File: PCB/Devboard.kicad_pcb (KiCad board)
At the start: 2 copper layers, 21 x 51 mm, 34 parts, among them J1 USB_C_Receptacle_USB2.0_14P, J2 Conn_01x20, J3 Conn_01x20, J4 Conn_01x03, SW1 SW_Push, U1 RP2040, U2 NCP1117-3.3_SOT223, U3 W25Q16JVZPIQ TR, Y1 12 MHz

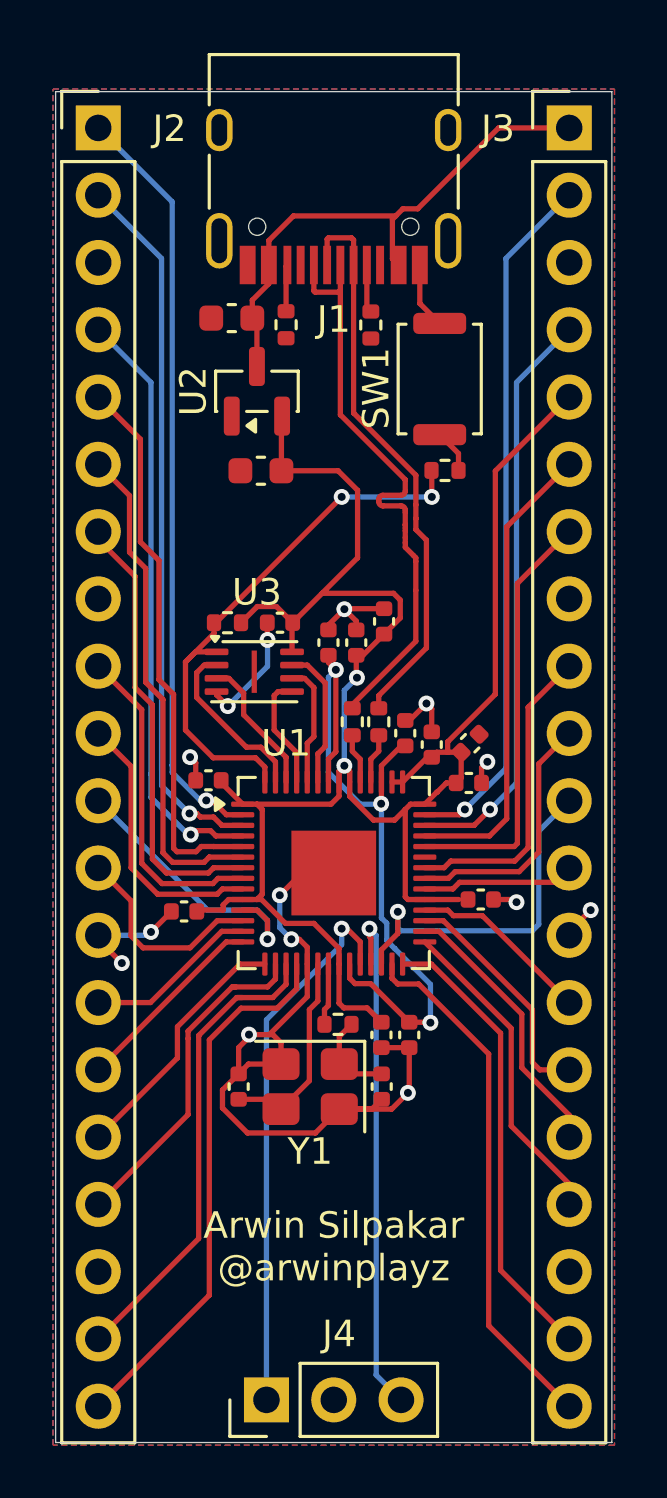
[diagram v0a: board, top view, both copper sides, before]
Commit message: added temperature sensor
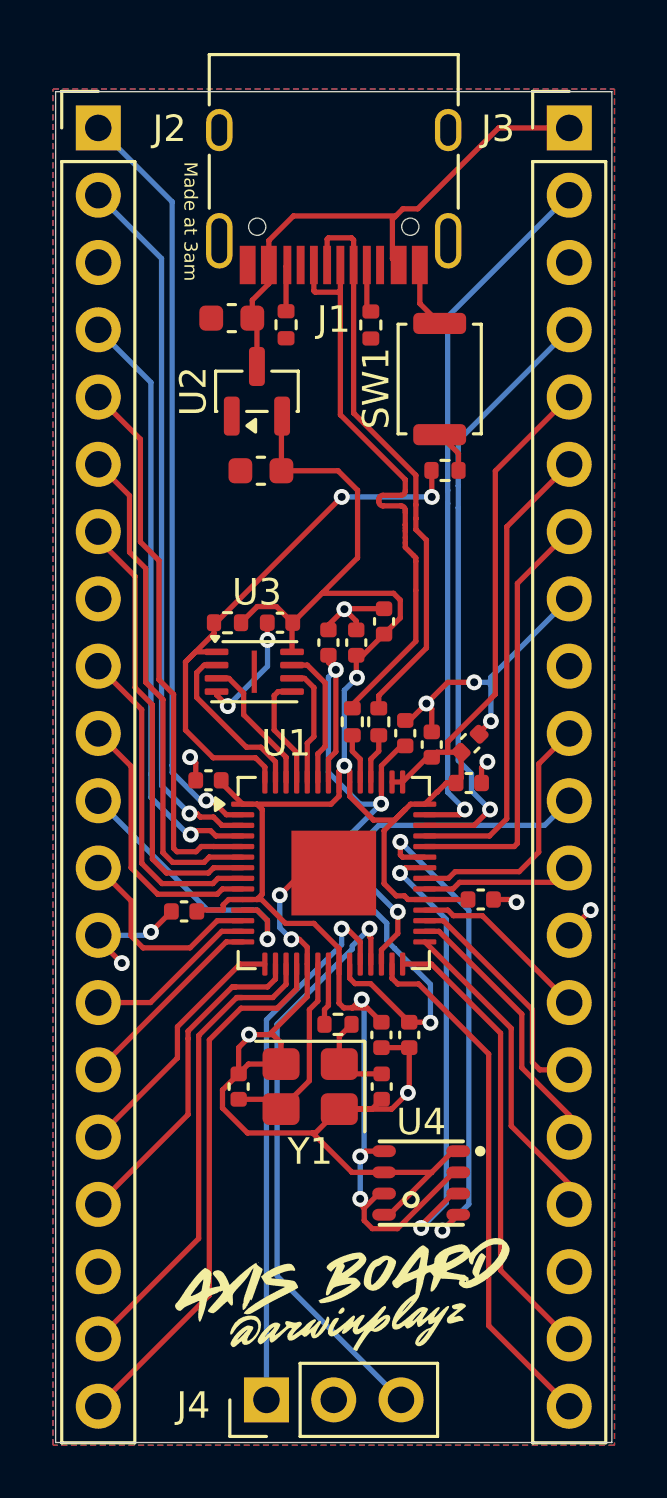
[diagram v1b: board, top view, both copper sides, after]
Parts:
- removed the G*** at (160.5, 118.3)
- added G***: LOGO, LOGO, F.Cu at (160.9, 135.0)
- added G***: LOGO, LOGO, B.Cu at (160.1, 114.9)
- added G***: LOGO, LOGO, B.Cu at (160.3, 134.9)
- added U4: BME680, lcsc2:LGA-8_L3.0-W3.0-P0.80-TR, F.Cu at (163.8, 131.2)
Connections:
- net +3V3 renamed TEMP_CSB
- J3 pad 9: GPIO24 -> unconnected-(J3-Pin_9-Pad9)
- U1 pad 36: GPIO24 -> TEMP_SDI
- U1 pad 37: unconnected-(U1-GPIO25-Pad37) -> TEMP_SCK
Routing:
- net TEMP_SCK: track 0.00 -> 18.5 mm, vias 0 -> 2
- net GND: track 50.2 -> 68.4 mm, vias 14 -> 16
- net TEMP_SDI: track 0.00 -> 17.1 mm, vias 0 -> 2
- net TEMP_CSB: track 76.8 -> 93.1 mm, vias 2 -> 5
- net GPIO24: track 11.7 -> 0.00 mm
- net SWD: track 19.6 -> 22.5 mm
- net GPIO28_ADC2: track 22.1 -> 23.1 mm
- net +1V1: track 27.5 -> 28.4 mm
- net GPIO29_ADC3: track 26.4 -> 27.0 mm
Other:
- board text added: "Made at 3am"
- board text removed: "Arwin Silpakar @arwinplayz"
- board text removed: "POWER"
